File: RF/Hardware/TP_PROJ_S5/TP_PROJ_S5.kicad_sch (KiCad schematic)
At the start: 7 parts, among them J2 DIN-5, J3 Batterie, U2 BU33SD5WG-TR

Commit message: Last footprints added and value changes
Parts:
- C1: footprint Capacitor_SMD:C_0603_1608Metric_Pad1.08x0.95mm_HandSolder -> Capacitor_SMD:C_0603_1608Metric
- C2: footprint Capacitor_SMD:C_0603_1608Metric_Pad1.08x0.95mm_HandSolder -> Capacitor_SMD:C_0402_1005Metric
- J2: footprint (none) -> footprints:DIN5_MIDI
- J3: footprint Connector_PinHeader_1.27mm:PinHeader_2x07_P1.27mm_Vertical -> Connector_JST:JST_XH_B2B-XH-A_1x02_P2.50mm_Vertical
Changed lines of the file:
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@@
 			)
 		)
-		(property "Footprint" ""
+		(property "Footprint" "footprints:DIN5_MIDI"
 			(at 72.39 93.98 0)
 			(effects
@@
 			)
 		)
-		(property "Footprint" "Capacitor_SMD:C_0603_1608Metric_Pad1.08x0.95mm_HandSolder"
+		(property "Footprint" "Capacitor_SMD:C_0603_1608Metric"
 			(at 28.2448 40.64 0)
 			(effects
@@
 			)
 		)
-		(property "Footprint" "Capacitor_SMD:C_0603_1608Metric_Pad1.08x0.95mm_HandSolder"
+		(property "Footprint" "Capacitor_SMD:C_0402_1005Metric"
 			(at 56.8452 40.64 0)
 			(effects
@@
 			)
 		)
-		(property "Footprint" "Connector_PinHeader_1.27mm:PinHeader_2x07_P1.27mm_Vertical"
+		(property "Footprint" "Connector_JST:JST_XH_B2B-XH-A_1x02_P2.50mm_Vertical"
 			(at 27.94 140.97 0)
 			(effects

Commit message: more footprints
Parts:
- removed J2: DIN-5, footprints:DIN5_MIDI, symbol Connector:DIN-5
- added D2: D, LED_SMD:LED_0603_1608Metric, symbol Device:D
- added IC1: SN7417N, footprints:DIP794W53P254L1930H508Q14N, symbol SN74:SN7417N
- added J4, J5: DIN-5, footprints:DIN5_MIDI, symbol Connector:DIN-5
- added R4, R6, R7: 220, Resistor_SMD:R_0805_2012Metric, symbol Device:R
- added R5: 270, Resistor_SMD:R_0805_2012Metric, symbol Device:R
- added U4: 6N138, footprints:DIP762W50P254L1018H450Q8, symbol Isolator:6N138
- D1: footprint LED_SMD:LED_0603_1608Metric_Pad1.05x0.95mm_HandSolder -> LED_SMD:LED_0603_1608Metric
- R1: footprint Resistor_SMD:R_0805_2012Metric_Pad1.20x1.40mm_HandSolder -> Resistor_SMD:R_0805_2012Metric
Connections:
- net +3.3V: now also R5.1, R7.2
- net GND: now also J5.2, U4.5 (GND)
- net stm32/RX_MIDI: now also R5.2, U4.6 (VO2)
- new net: D2.1 (K), R4.2, U4.2 (C1)
- new net: D2.2 (A), J4.5, U4.3 (C2)
- new net: J4.4, R4.1
- new net: J5.5, R6.1
- new net: J5.4, R7.1
- no-connect marks 4 -> 7
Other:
- moved on the sheet: C1, C2, D1, R1, U2

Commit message: final steps before routing
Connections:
- net GND: now also IC1.7 (GND)
- net stm32/TX_MIDI: now also IC1.2 (1Y)
- net at IC1.1 (1A): now also R6.2
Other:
- moved on the sheet: IC1
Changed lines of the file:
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@@
+	(wire
+		(pts
+			(xy 57.15 73.66) (xy 57.15 77.47)
+		)
+		(stroke
+			(width 0)
+			(type default)
+		)
+	)
 	(wire
 		(pts
@@
 	(wire
 		(pts
+			(xy 54.61 77.47) (xy 54.61 73.66)
+		)
+		(stroke
+			(width 0)
+			(type default)
+		)
+	)
+	(wire
+		(pts
 			(xy 29.21 30.48) (xy 29.21 33.02)
 		)
@@
 		(pts
 			(xy 36.83 67.31) (xy 35.56 67.31)
+		)
+		(stroke
+			(width 0)
+			(type default)
+		)
+	)
+	(wire
+		(pts
+			(xy 44.45 77.47) (xy 54.61 77.47)
+		)
+		(stroke
+			(width 0)
+			(type default)
+		)
+	)
+	(wire
+		(pts
+			(xy 57.15 77.47) (xy 80.01 77.47)
 		)
 		(stroke
@@
 	(symbol
 		(lib_id "SN74:SN7417N")
-		(at 50.8 60.96 0)
+		(at 54.61 73.66 90)
 		(unit 1)
 		(exclude_from_sim no)
@@
 		(fields_autoplaced yes)
 		(property "Reference" "IC1"
-			(at 63.5 53.34 0)
-			(effects
-				(font
-					(size 1.27 1.27)
-				)
+			(at 73.66 59.6899 90)
+			(effects
+				(font
+					(size 1.27 1.27)
+				)
+				(justify right)
 			)
 		)
 		(property "Value" "SN7417N"
-			(at 63.5 55.88 0)
-			(effects
-				(font
-					(size 1.27 1.27)
-				)
+			(at 73.66 62.2299 90)
+			(effects
+				(font
+					(size 1.27 1.27)
+				)
+				(justify right)
 			)
 		)
 		(property "Footprint" "footprints:DIP794W53P254L1930H508Q14N"
-			(at 72.39 155.88 0)
+			(at 149.53 52.07 0)
 			(effects
 				(font
@@
 		)
 		(property "Datasheet" "http://www.ti.com/lit/gpn/sn7417"
-			(at 72.39 255.88 0)
+			(at 249.53 52.07 0)
 			(effects
 				(font
@@
 		)
 		(property "Description" "Hex Buffers/Drivers With Open-Collector High-Voltage Outputs"
-			(at 50.8 60.96 0)
+			(at 54.61 73.66 0)
 			(effects
 				(font
@@
 		)
 		(property "Height" "5.08"
-			(at 72.39 455.88 0)
+			(at 449.53 52.07 0)
 			(effects
 				(font
@@
 		)
 		(property "Manufacturer_Name" "Texas Instruments"
-			(at 72.39 555.88 0)
+			(at 549.53 52.07 0)
 			(effects
 				(font
@@
 		)
 		(property "Manufacturer_Part_Number" "SN7417N"
-			(at 72.39 655.88 0)
+			(at 649.53 52.07 0)
 			(effects
 				(font
@@
 		)
 		(property "Mouser Part Number" "595-SN7417N"
-			(at 72.39 755.88 0)
+			(at 749.53 52.07 0)
 			(effects
 				(font
@@
 		)
 		(property "Mouser Price/Stock" "https://www.mouser.co.uk/ProductDetail/Texas-Instruments/SN7417N?qs=rgxfVHSNRPW2P%252BfiJNxH%2FA%3D%3D"
-			(at 72.39 855.88 0)
+			(at 849.53 52.07 0)
 			(effects
 				(font
@@
 		)
 		(property "Arrow Part Number" "SN7417N"
-			(at 72.39 955.88 0)
+			(at 949.53 52.07 0)
 			(effects
 				(font
@@
 		)
 		(property "Arrow Price/Stock" "https://www.arrow.com/en/products/sn7417n/texas-instruments?region=nac"
-			(at 72.39 1055.88 0)
+			(at 1049.53 52.07 0)
 			(effects
 				(font
@@
 					(unit 1)
 				)
+			)
+		)
+	)
+	(symbol
+		(lib_id "power:GND")
+		(at 69.85 73.66 0)
+		(unit 1)
+		(exclude_from_sim no)
+		(in_bom yes)
+		(on_board yes)
+		(dnp no)
+		(property "Reference" "#PWR032"
+			(at 69.85 80.01 0)
+			(effects
+				(font
+					(size 1.27 1.27)
+				)
+				(hide yes)
+			)
+		)
+		(property "Value" "GND"
+			(at 72.898 73.66 0)
+			(effects
+				(font
+					(size 1.27 1.27)
+				)
+			)
+		)
+		(property "Footprint" ""
+			(at 69.85 73.66 0)
+			(effects
+				(font
+					(size 1.27 1.27)
+				)
+				(hide yes)
+			)
+		)
+		(property "Datasheet" ""
+			(at 69.85 73.66 0)
+			(effects
+				(font
+					(size 1.27 1.27)
+				)
+				(hide yes)
+			)
+		)
+		(property "Description" "Power symbol creates a global label with name \"GND\" , ground"
+			(at 69.85 73.66 0)
+			(effects
+				(font
+					(size 1.27 1.27)
+				)
+				(hide yes)
+			)
+		)
+		(pin "1"
+		)
+		(instances
+			(project ""
+				(path "/5e74dd86-eabf-4eac-a6ab-2534adeb335f"
+					(reference "#PWR032")
+					(unit 1)
+				)

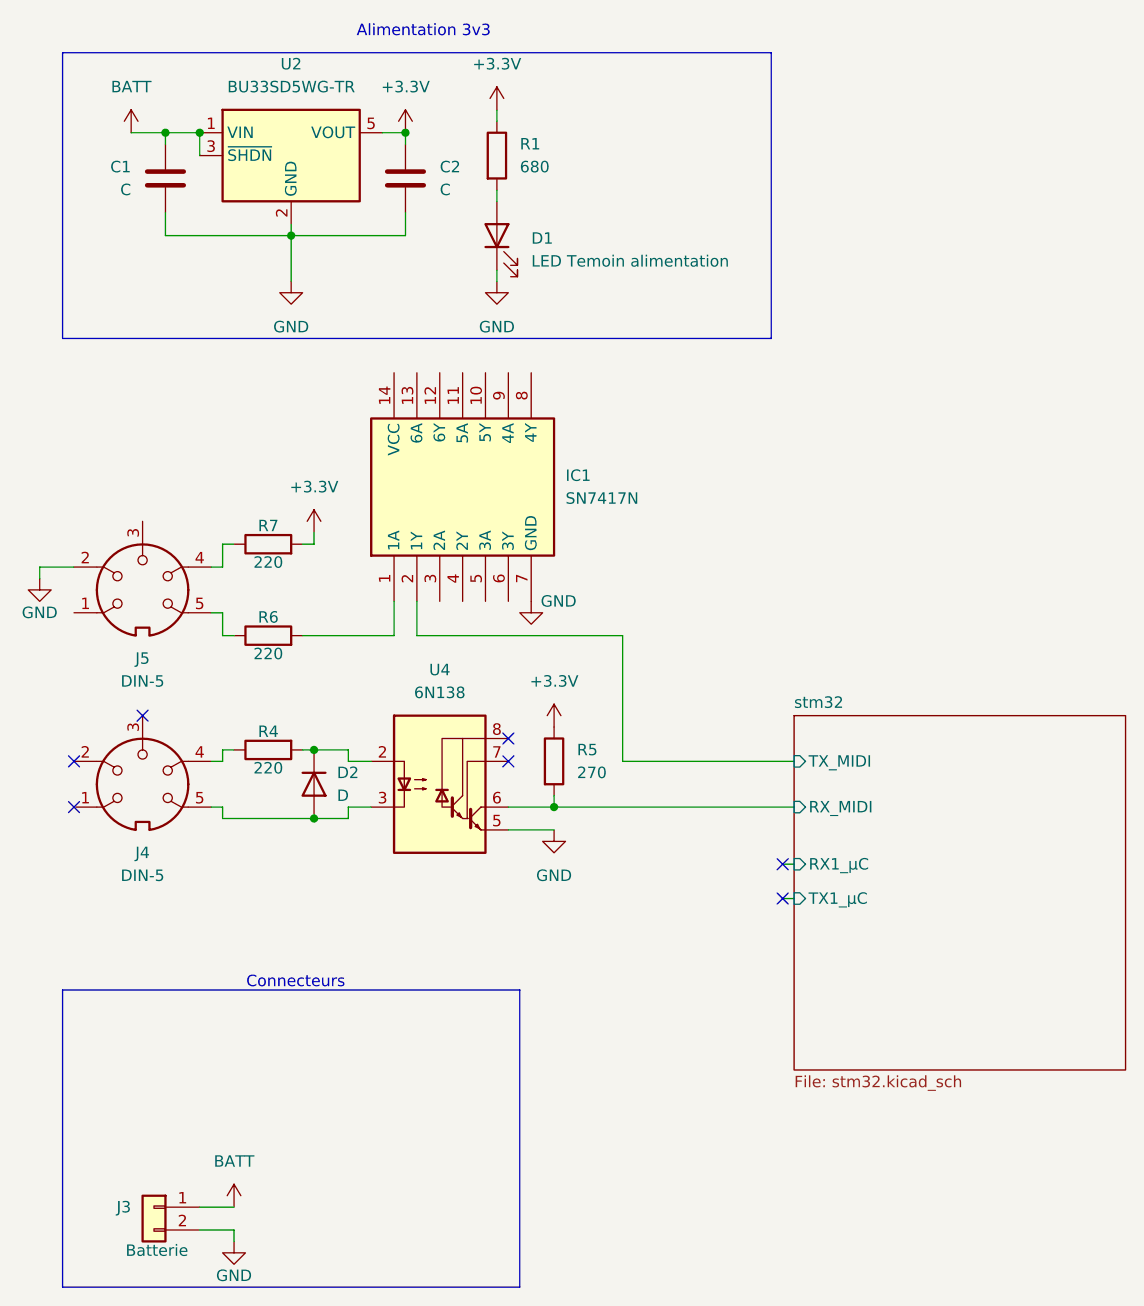
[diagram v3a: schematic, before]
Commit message: Schematic changes
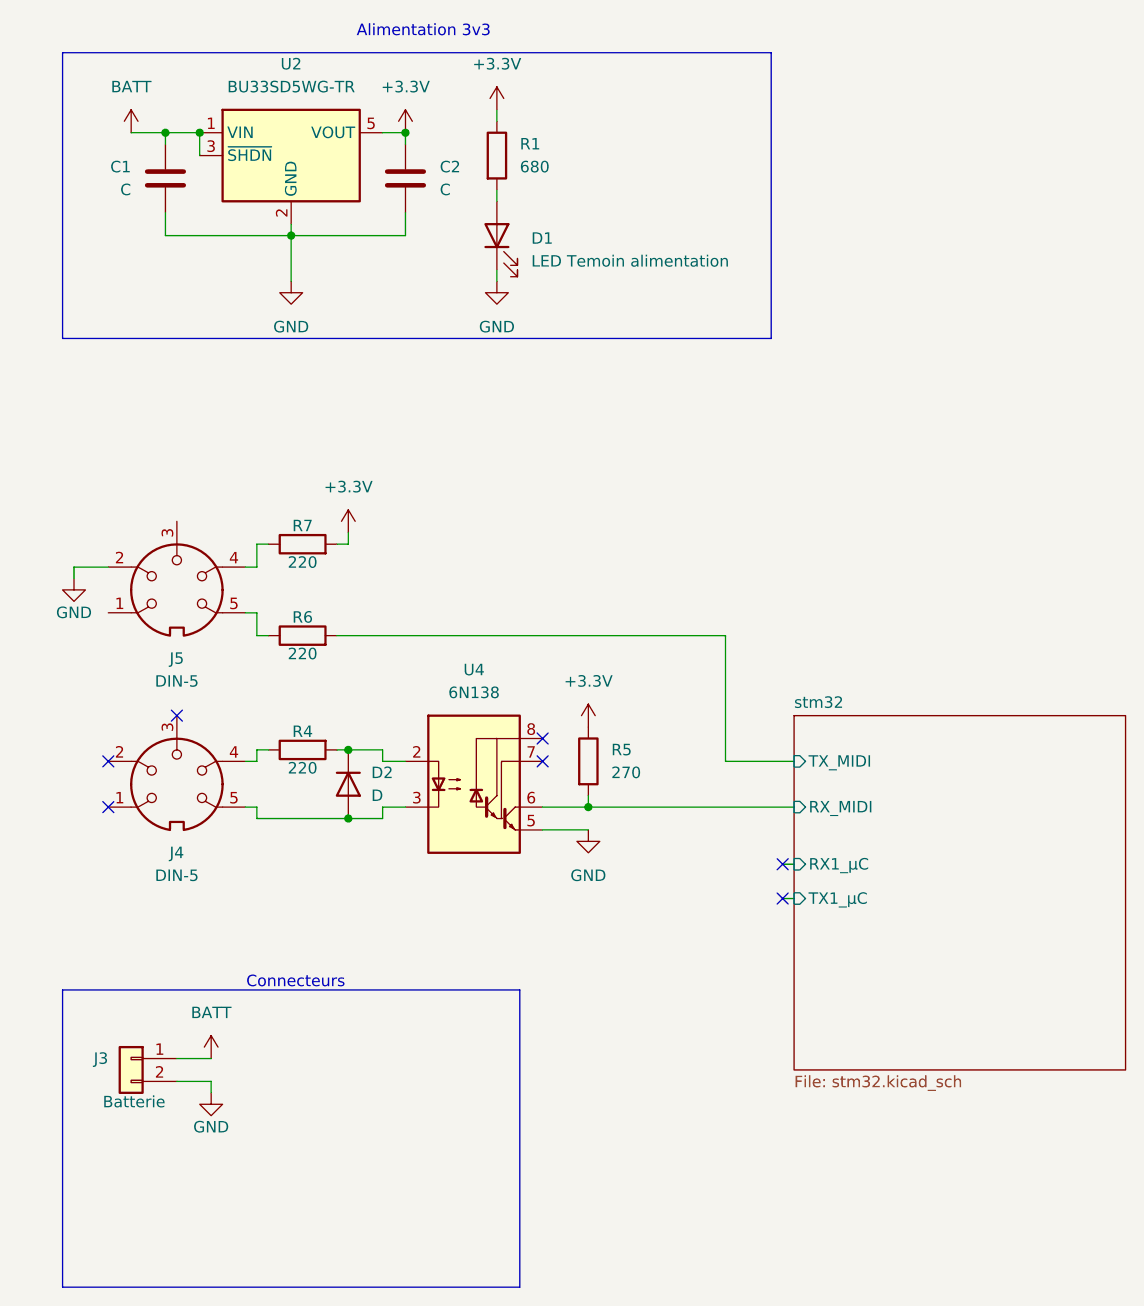
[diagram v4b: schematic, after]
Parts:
- removed IC1: SN7417N, footprints:DIP794W53P254L1930H508Q14N, symbol SN74:SN7417N
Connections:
- net stm32/TX_MIDI: now also R6.2
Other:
- moved on the sheet: D2, J3, J4, J5, R4, R5, R6, R7, U4
